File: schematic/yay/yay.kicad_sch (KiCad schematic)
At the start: 7 parts, among them SW1 SW_SPDT, SW2 SW_Push, U1 xiao esp32-s3 sense, U2 IP2312 Li-Ion charger 4.2V

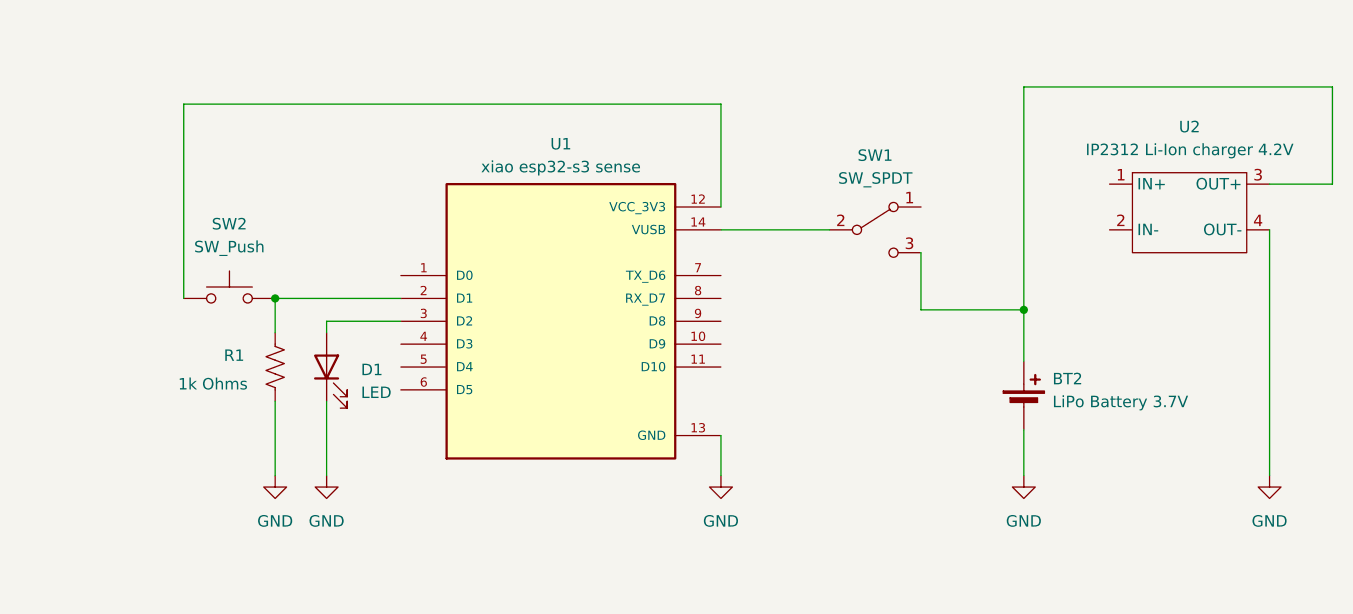
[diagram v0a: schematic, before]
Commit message: added state machine; video capabilities
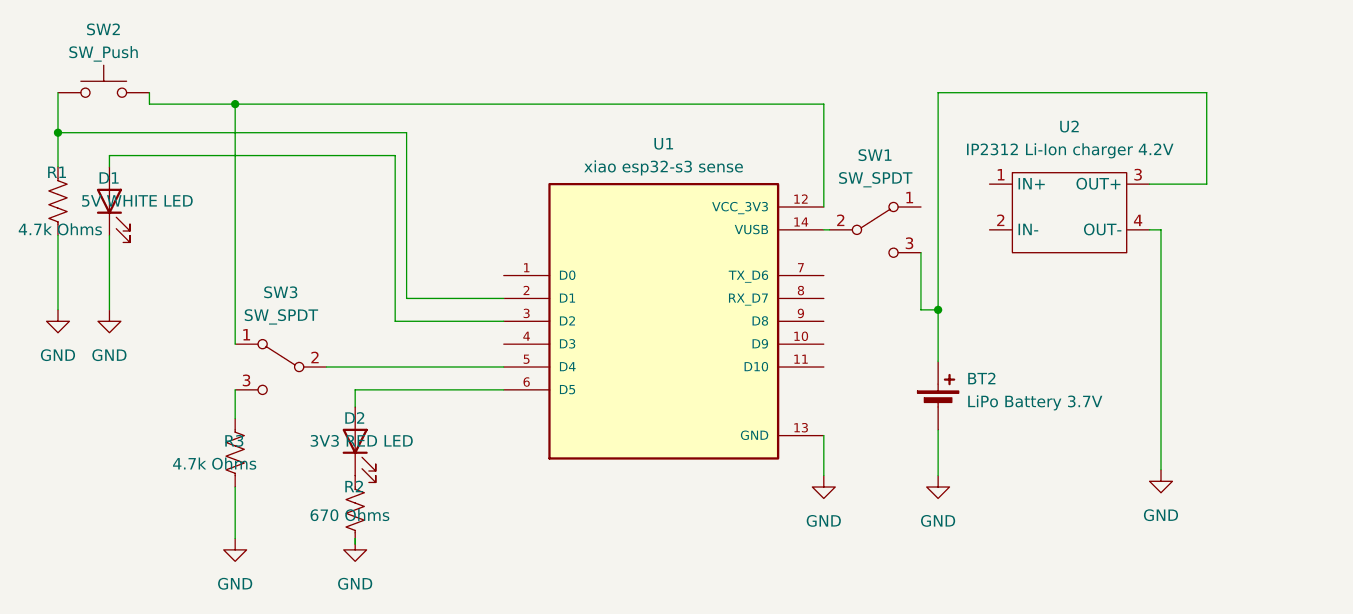
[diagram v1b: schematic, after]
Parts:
- added D2: 3V3 RED LED, symbol Device:LED
- added R2: 670 Ohms, symbol Device:R_US
- added R3: 4.7k Ohms, symbol Device:R_US
- added SW3: SW_SPDT, symbol Switch:SW_SPDT
- D1: value LED -> 5V WHITE LED
- R1: value 1k Ohms -> 4.7k Ohms
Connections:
- net GND: now also R2.2, R3.2
- net at U1.12 (VCC_3V3): now also SW2.2, SW3.1 (A); no longer SW2.1
- net at R1.1, U1.2 (D1): now also SW2.1; no longer SW2.2
- net at U1.5 (D4): now also SW3.2 (B)
- net at U1.6 (D5): now also D2.2 (A)
- new net: D2.1 (K), R2.1
- new net: R3.1, SW3.3 (C)
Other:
- moved on the sheet: BT2, D1, R1, SW2, U1, U2

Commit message: upload but camera heating much? + not writing images
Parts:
- added BT1: LiPo Battery 3.7V, symbol Device:Battery_Cell
- added D3: 5V WHITE LED, symbol Device:LED
- added R4: 4.7k Ohms, symbol Device:R_US
- added SW4: SW_Push, symbol Switch:SW_Push
- added SW6: SW_SPDT, symbol Switch:SW_SPDT
- added U3: xiao esp32-s3 sense, 113991054:MODULE_113991054, symbol 113991054:113991054
- added U4: IP2312 Li-Ion charger 4.2V, Battery:BatteryHolder_Keystone_2460_1xAA, symbol li-ion_charger:IP2312_Li-Ion_charger
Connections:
- net GND: now also BT1.2 (-), D3.1 (K), R4.2, U3.13 (GND), U4.4 (OUT-)
- new net: SW4.2, U3.12 (VCC_3V3)
- new net: SW6.2 (B), U3.14 (VUSB)
- new net: R4.1, SW4.1, U3.2 (D1)
- new net: D3.2 (A), U3.3 (D2)
- new net: BT1.1 (+), SW6.3 (C), U4.3 (OUT+)
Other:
- note added: "VERSION 1 WITH PICTURING & RECORDING"
- note added: "VERSION 2 PICTURING ONLY"
- moved on the sheet: BT2, D1, D2, R1, R2, R3, SW1, SW2, SW3, U1, U2

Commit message: more 3d updates
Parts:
- added BT3: LiPo Battery 3.7V, symbol Device:Battery_Cell
- added D4, D5: 5V WHITE LED, symbol Device:LED
- added SW5: SW_Reed, symbol Switch:SW_Reed
- added U5: IP2312 Li-Ion charger 4.2V, Battery:BatteryHolder_Keystone_2460_1xAA, symbol li-ion_charger:IP2312_Li-Ion_charger
- added U6: ~, symbol LED_vustom:LD06AJSA_led_driver
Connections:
- net GND: now also BT3.2 (-), D4.1 (K), D5.1 (K), U5.4 (OUT-), U6. (V1)
- new net: BT3.1 (+), SW5.2, U5.3 (OUT+)
- new net: SW5.1, U6. (V1)
- new net: D4.2 (A), D5.2 (A), U6. (V1)
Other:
- moved on the sheet: BT1, SW6, U4
